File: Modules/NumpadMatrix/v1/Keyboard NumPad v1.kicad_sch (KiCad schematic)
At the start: 43 parts, among them U2 ESP32-C3_SUPERMINI_SMD

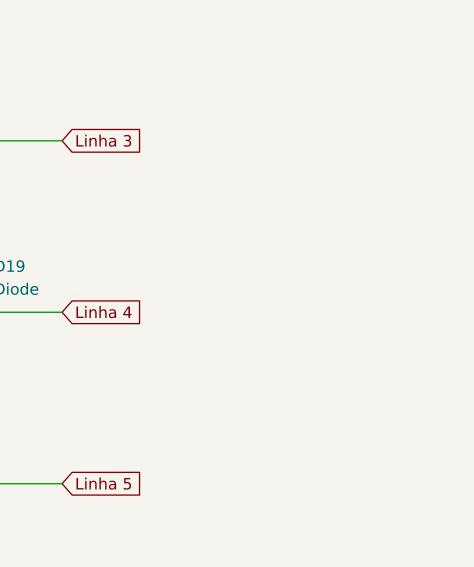
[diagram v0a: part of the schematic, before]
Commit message: iniciated the ControlerBoard V0. I need the screen size!!
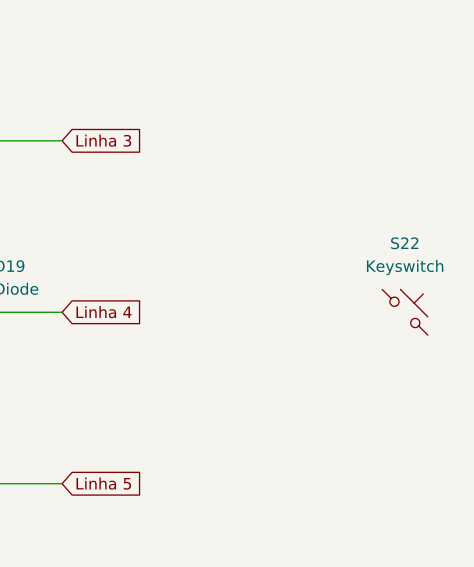
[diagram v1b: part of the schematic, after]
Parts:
- added S22: Keyswitch, Keebio-Parts:Cherry-MX-Low-Profile, symbol ScottoKeebs:Placeholder_Keyswitch
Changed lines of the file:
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@@
+	)
+	(symbol
+		(lib_id "ScottoKeebs:Placeholder_Keyswitch")
+		(at 191.77 125.73 0)
+		(unit 1)
+		(exclude_from_sim no)
+		(in_bom yes)
+		(on_board yes)
+		(dnp no)
+		(fields_autoplaced yes)
+		(property "Reference" "S22"
+			(at 191.77 118.11 0)
+			(effects
+				(font
+					(size 1.27 1.27)
+				)
+			)
+		)
+		(property "Value" "Keyswitch"
+			(at 191.77 120.65 0)
+			(effects
+				(font
+					(size 1.27 1.27)
+				)
+			)
+		)
+		(property "Footprint" "Keebio-Parts:Cherry-MX-Low-Profile"
+			(at 191.77 125.73 0)
+			(effects
+				(font
+					(size 1.27 1.27)
+				)
+				(hide yes)
+			)
+		)
+		(property "Datasheet" "~"
+			(at 191.77 125.73 0)
+			(effects
+				(font
+					(size 1.27 1.27)
+				)
+				(hide yes)
+			)
+		)
+		(property "Description" "Push button switch, normally open, two pins, 45° tilted"
+			(at 191.77 125.73 0)
+			(effects
+				(font
+					(size 1.27 1.27)
+				)
+				(hide yes)
+			)
+		)
+		(pin "1"
+		)
+		(pin "2"
+		)
+		(instances
+			(project "Keyboard NumPad v1"
+				(path "/72d6a7bc-74bb-4585-b459-4dd0fcbeadc8"
+					(reference "S22")
+					(unit 1)
+				)
+			)
+		)
 	)
 	(symbol
